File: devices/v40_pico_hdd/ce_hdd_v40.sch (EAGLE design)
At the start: 110 parts, among them IC1 RASPBERRY_PICOSMD-TH, IC101 74LVC245AT20-13, IC2 74LVC245AT20-13, IC201 74LVC245AT20-13, IC202 74LVC373APW,118, IC203 74LVC373APW,118, IC204 AZ1117H-ADJTRE1, IC3 74LVC245AT20-13, IC4 TLV1117LV33DCYR, IC5 74LVC245AT20-13, IC6 74AHCT1G08GW,125, J101 M19, J2 USB4125-GF-A, J201 TE Connectivity - 5173280-3, J203 ZL231-50PG, Q201 FDV304P, Q202 FDV304P, Q203 FDV304P, Q204 FDV304P, Q205 FDV304P, Q206 FDV304P, Q207 FDV304P, Q208 FDV304P, Q209 FDV304P, Q210 FDV304P, Q211 FDV304P, Q212 FDV304P, Q213 FDV304P, Q214 FDV304P, Q215 FDV304P, Q216 FDV304P, Q217 FDV304P, Q218 FDV304P, SW1 SMSR-1

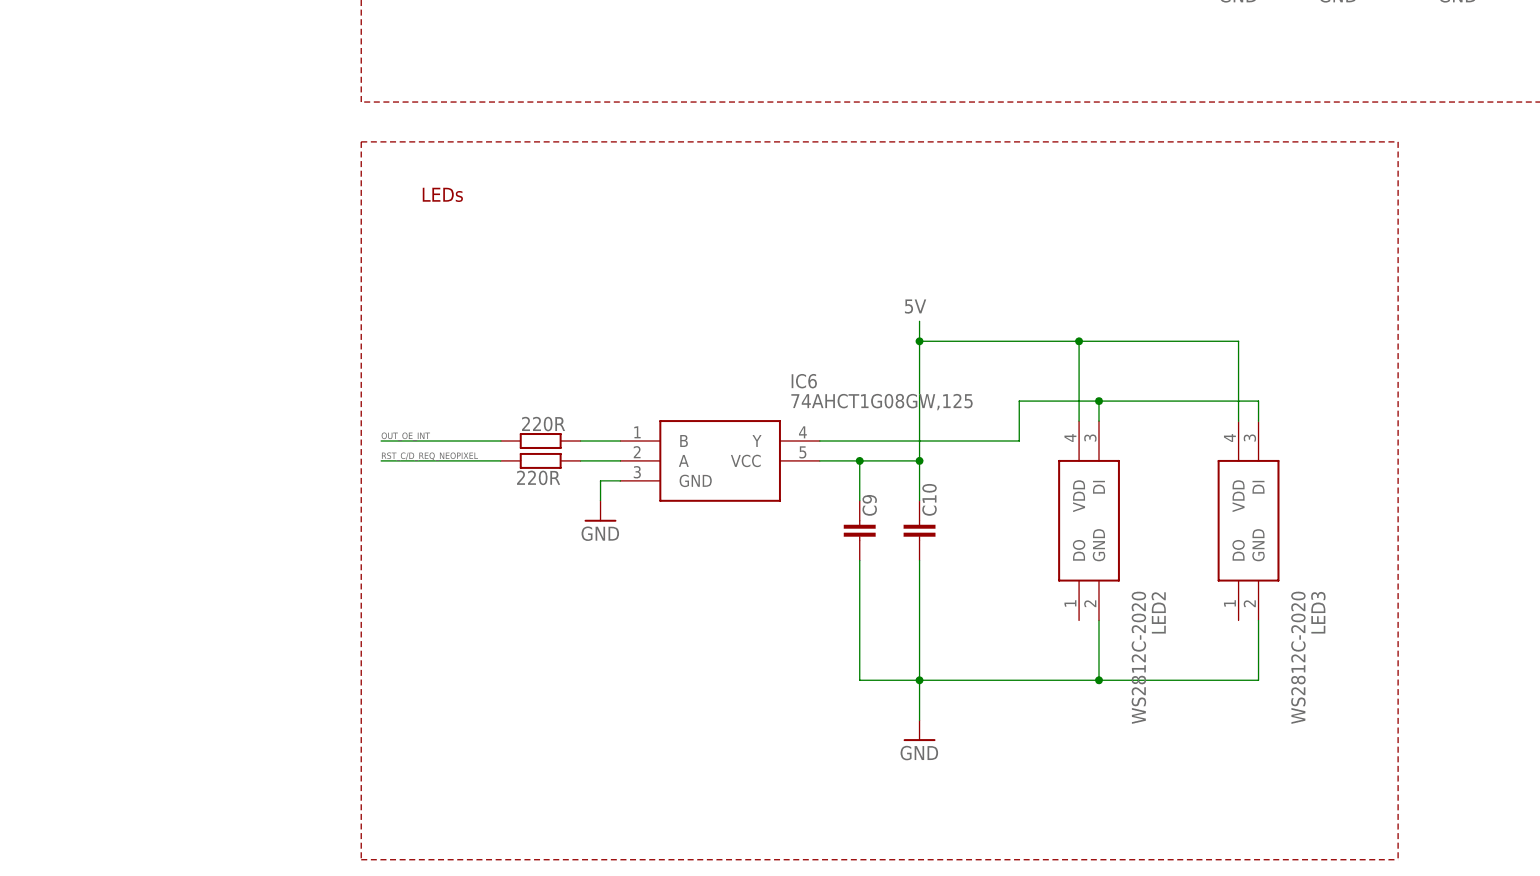
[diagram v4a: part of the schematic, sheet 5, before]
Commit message: fix for SCSI neopixel colors during start / run
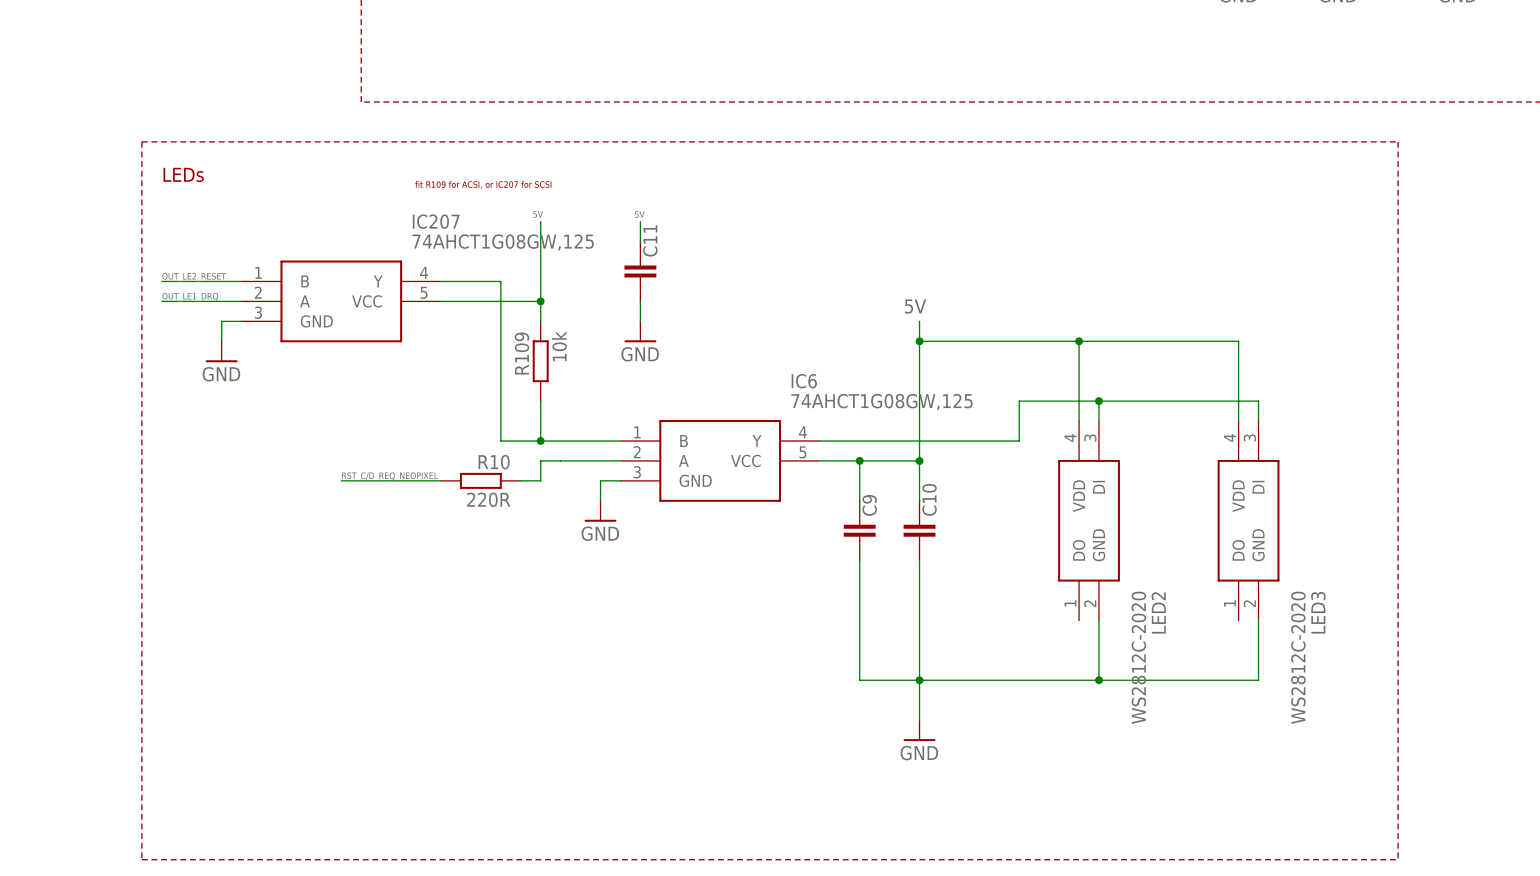
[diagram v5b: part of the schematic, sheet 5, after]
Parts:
- removed R9: 220R, rcl:R-EU_R0603
- added C11: 100 nF, rcl:C-EUC0603
- added IC207: 74AHCT1G08GW,125, 74AHCT1G08GW_125:74AHCT1G08GW,125
- added R109: 10k, rcl:R-EU_R0603
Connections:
- net 5V: now also C11.1, IC207.VCC, R109.1
- net GND: now also C11.2, IC207.GND
- net N$4: now also IC207.Y, R109.2; no longer R9.2
- net OUT_LE1_DRQ: now also IC207.A
- net OUT_LE2_RESET: now also IC207.B
- net OUT_OE_INT: no longer R9.1
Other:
- note added: "fit R109 for ACSI, or IC207 for SCSI"
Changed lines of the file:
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@@
 <part name="R8" library="rcl" deviceset="R-EU_" device="R0603" value="10k"/>
 <part name="IC6" library="74AHCT1G08GW_125" deviceset="74AHCT1G08GW,125" device=""/>
-<part name="R9" library="rcl" deviceset="R-EU_" device="R0603" value="220R"/>
 <part name="D101" library="BAT54WSTR" deviceset="BAT54WSTR" device="">
 <variant name="SCSI" populate="no"/>
@@
 <variant name="SCSI" populate="no"/>
 </part>
+<part name="IC207" library="74AHCT1G08GW_125" deviceset="74AHCT1G08GW,125" device="">
+<attribute name="DESCRIPTION" value="74AHC(T)1G08 - 2-input AND gate@en-us"/>
+<attribute name="HEIGHT" value="1.1mm"/>
+<attribute name="MANUFACTURER_NAME" value="Nexperia"/>
+<attribute name="MANUFACTURER_PART_NUMBER" value="74AHCT1G08GW,125"/>
+<attribute name="TME_ELECTRONIC_COMPONENTS_PART_NUMBER" value=""/>
+<attribute name="TME_ELECTRONIC_COMPONENTS_PRICE-STOCK" value=""/>
+<variant name="ACSI" populate="no"/>
+</part>
+<part name="GND22" library="supply1" deviceset="GND" device=""/>
+<part name="R109" library="rcl" deviceset="R-EU_" device="R0603" value="10k">
+<variant name="SCSI" populate="no" value="220R"/>
+</part>
+<part name="C11" library="rcl" deviceset="C-EU" device="C0603" value="100 nF"/>
+<part name="GND23" library="supply1" deviceset="GND" device=""/>
 </parts>
 <sheets>
@@
 <wire x1="109.22" y1="88.9" x2="109.22" y2="231.14" width="0.1524" layer="94" style="shortdash"/>
 <text x="116.84" y="223.52" size="2.54" layer="94" font="vector">power supply</text>
-<wire x1="109.22" y1="83.82" x2="241.3" y2="83.82" width="0.1524" layer="94" style="shortdash"/>
-<wire x1="109.22" y1="83.82" x2="109.22" y2="-7.62" width="0.1524" layer="94" style="shortdash"/>
+<wire x1="81.28" y1="83.82" x2="241.3" y2="83.82" width="0.1524" layer="94" style="shortdash"/>
+<wire x1="81.28" y1="83.82" x2="81.28" y2="-7.62" width="0.1524" layer="94" style="shortdash"/>
 <wire x1="241.3" y1="83.82" x2="241.3" y2="-7.62" width="0.1524" layer="94" style="shortdash"/>
-<wire x1="109.22" y1="-7.62" x2="241.3" y2="-7.62" width="0.1524" layer="94" style="shortdash"/>
+<wire x1="81.28" y1="-7.62" x2="241.3" y2="-7.62" width="0.1524" layer="94" style="shortdash"/>
 <text x="-63.5" y="116.078" size="0.8128" layer="91" font="vector" ratio="10">If using W6100, GP15 and GP22 can be used for IKBD</text>
 <text x="-63.5" y="114.3" size="0.8128" layer="94" font="vector" ratio="10">If using W6300, GP15 and GP22 are used by W6300 and IKBD cannot use them.</text>
@@
 <text x="79.502" y="154.178" size="0.8128" layer="91" font="vector" rot="R90">fit for ACSI</text>
 <text x="79.502" y="138.43" size="0.8128" layer="91" font="vector" rot="R90">fit for SCSI</text>
-<text x="116.84" y="76.2" size="1.778" layer="94">LEDs</text>
+<text x="83.82" y="78.74" size="1.778" layer="94">LEDs</text>
+<text x="116.078" y="77.978" size="0.8128" layer="94" font="vector">fit R109 for ACSI, or IC207 for SCSI</text>
 </plain>
 <instances>
@@
 </instance>
 <instance part="GND11" gate="1" x="76.2" y="132.08"/>
-<instance part="R10" gate="G$1" x="132.08" y="43.18" smashed="yes" rot="MR0">
-<attribute name="VALUE" x="134.62" y="40.132" size="1.778" layer="96" rot="MR0"/>
-</instance>
+<instance part="R10" gate="G$1" x="124.46" y="40.64" rot="MR0"/>
 <instance part="SW1" gate="G$1" x="198.12" y="137.16"/>
 <instance part="LED3" gate="G$1" x="223.52" y="48.26" rot="R270"/>
@@
 </instance>
 <instance part="IC6" gate="G$1" x="142.24" y="45.72"/>
-<instance part="R9" gate="G$1" x="132.08" y="45.72" smashed="yes" rot="MR180">
-<attribute name="VALUE" x="129.54" y="48.768" size="1.778" layer="96" rot="MR180"/>
+<instance part="IC207" gate="G$1" x="93.98" y="66.04"/>
+<instance part="GND22" gate="1" x="91.44" y="55.88"/>
+<instance part="R109" gate="G$1" x="132.08" y="55.88" rot="MR270"/>
+<instance part="C11" gate="G$1" x="144.78" y="68.58" smashed="yes">
+<attribute name="NAME" x="146.939" y="69.088" size="1.778" layer="95" rot="R90"/>
 </instance>
+<instance part="GND23" gate="1" x="144.78" y="58.42"/>
 </instances>
 <busses>
@@
 <wire x1="76.2" y1="137.16" x2="76.2" y2="134.62" width="0.1524" layer="91"/>
 </segment>
+<segment>
+<pinref part="IC207" gate="G$1" pin="GND"/>
+<pinref part="GND22" gate="1" pin="GND"/>
+<wire x1="93.98" y1="60.96" x2="91.44" y2="60.96" width="0.1524" layer="91"/>
+<wire x1="91.44" y1="60.96" x2="91.44" y2="58.42" width="0.1524" layer="91"/>
+</segment>
+<segment>
+<pinref part="C11" gate="G$1" pin="2"/>
+<pinref part="GND23" gate="1" pin="GND"/>
+<wire x1="144.78" y1="63.5" x2="144.78" y2="60.96" width="0.1524" layer="91"/>
+</segment>
 </net>
 <net name="5V" class="0">
@@
 <pinref part="IC6" gate="G$1" pin="VCC"/>
 </segment>
+<segment>
+<pinref part="IC207" gate="G$1" pin="VCC"/>
+<wire x1="119.38" y1="63.5" x2="132.08" y2="63.5" width="0.1524" layer="91"/>
+<wire x1="132.08" y1="63.5" x2="132.08" y2="73.66" width="0.1524" layer="91"/>
+<label x="131.064" y="74.168" size="0.8128" layer="95" font="vector"/>
+<pinref part="R109" gate="G$1" pin="1"/>
+<wire x1="132.08" y1="60.96" x2="132.08" y2="63.5" width="0.1524" layer="91"/>
+<junction x="132.08" y="63.5"/>
+</segment>
+<segment>
+<pinref part="C11" gate="G$1" pin="1"/>
+<wire x1="144.78" y1="71.12" x2="144.78" y2="73.66" width="0.1524" layer="91"/>
+<label x="144.018" y="74.168" size="0.8128" layer="95" font="vector"/>
+</segment>
 </net>
 <net name="N$1" class="0">
@@
 <segment>
 <pinref part="R10" gate="G$1" pin="2"/>
-<wire x1="127" y1="43.18" x2="111.76" y2="43.18" width="0.1524" layer="91"/>
-<label x="111.76" y="43.434" size="0.8128" layer="95" font="vector"/>
+<wire x1="119.38" y1="40.64" x2="106.68" y2="40.64" width="0.1524" layer="91"/>
+<label x="106.68" y="40.894" size="0.8128" layer="95" font="vector"/>
 </segment>
 </net>
@@
 <pinref part="R8" gate="G$1" pin="2"/>
 </segment>
+<segment>
+<pinref part="IC207" gate="G$1" pin="A"/>
+<wire x1="93.98" y1="63.5" x2="83.82" y2="63.5" width="0.1524" layer="91"/>
+<label x="83.82" y="63.754" size="0.8128" layer="95" font="vector"/>
+</segment>
 </net>
 <net name="SEL_I/O_DP_A1" class="0">
@@
 <pinref part="R7" gate="G$1" pin="2"/>
 </segment>
-<segment>
-<pinref part="R9" gate="G$1" pin="1"/>
-<wire x1="127" y1="45.72" x2="111.76" y2="45.72" width="0.1524" layer="91"/>
-<label x="111.76" y="45.974" size="0.8128" layer="95" font="vector"/>
-</segment>
 </net>
 <net name="OUT_LE2_RESET" class="0">
@@
 <label x="-18.796" y="127.254" size="0.8128" layer="95" font="vector"/>
 </segment>
+<segment>
+<pinref part="IC207" gate="G$1" pin="B"/>
+<wire x1="93.98" y1="66.04" x2="83.82" y2="66.04" width="0.1524" layer="91"/>
+<label x="83.82" y="66.294" size="0.8128" layer="95" font="vector"/>
+</segment>
 </net>
 <net name="KEYB_RX" class="0">
@@
 <segment>
 <pinref part="R10" gate="G$1" pin="1"/>
-<wire x1="137.16" y1="43.18" x2="142.24" y2="43.18" width="0.1524" layer="91"/>
+<wire x1="129.54" y1="40.64" x2="132.08" y2="40.64" width="0.1524" layer="91"/>
+<wire x1="132.08" y1="40.64" x2="132.08" y2="43.18" width="0.1524" layer="91"/>
+<wire x1="132.08" y1="43.18" x2="134.62" y2="43.18" width="0.1524" layer="91"/>
+<wire x1="134.62" y1="43.18" x2="142.24" y2="43.18" width="0.1524" layer="91"/>
 <pinref part="IC6" gate="G$1" pin="A"/>
 </segment>
@@
 <segment>
 <pinref part="IC6" gate="G$1" pin="B"/>
-<pinref part="R9" gate="G$1" pin="2"/>
-<wire x1="142.24" y1="45.72" x2="137.16" y2="45.72" width="0.1524" layer="91"/>
+<pinref part="IC207" gate="G$1" pin="Y"/>
+<wire x1="119.38" y1="66.04" x2="127" y2="66.04" width="0.1524" layer="91"/>
+<wire x1="127" y1="66.04" x2="127" y2="45.72" width="0.1524" layer="91"/>
+<wire x1="127" y1="45.72" x2="132.08" y2="45.72" width="0.1524" layer="91"/>
+<pinref part="R109" gate="G$1" pin="2"/>
+<wire x1="132.08" y1="45.72" x2="142.24" y2="45.72" width="0.1524" layer="91"/>
+<wire x1="132.08" y1="50.8" x2="132.08" y2="45.72" width="0.1524" layer="91"/>
+<junction x="132.08" y="45.72"/>
 </segment>
 </net>

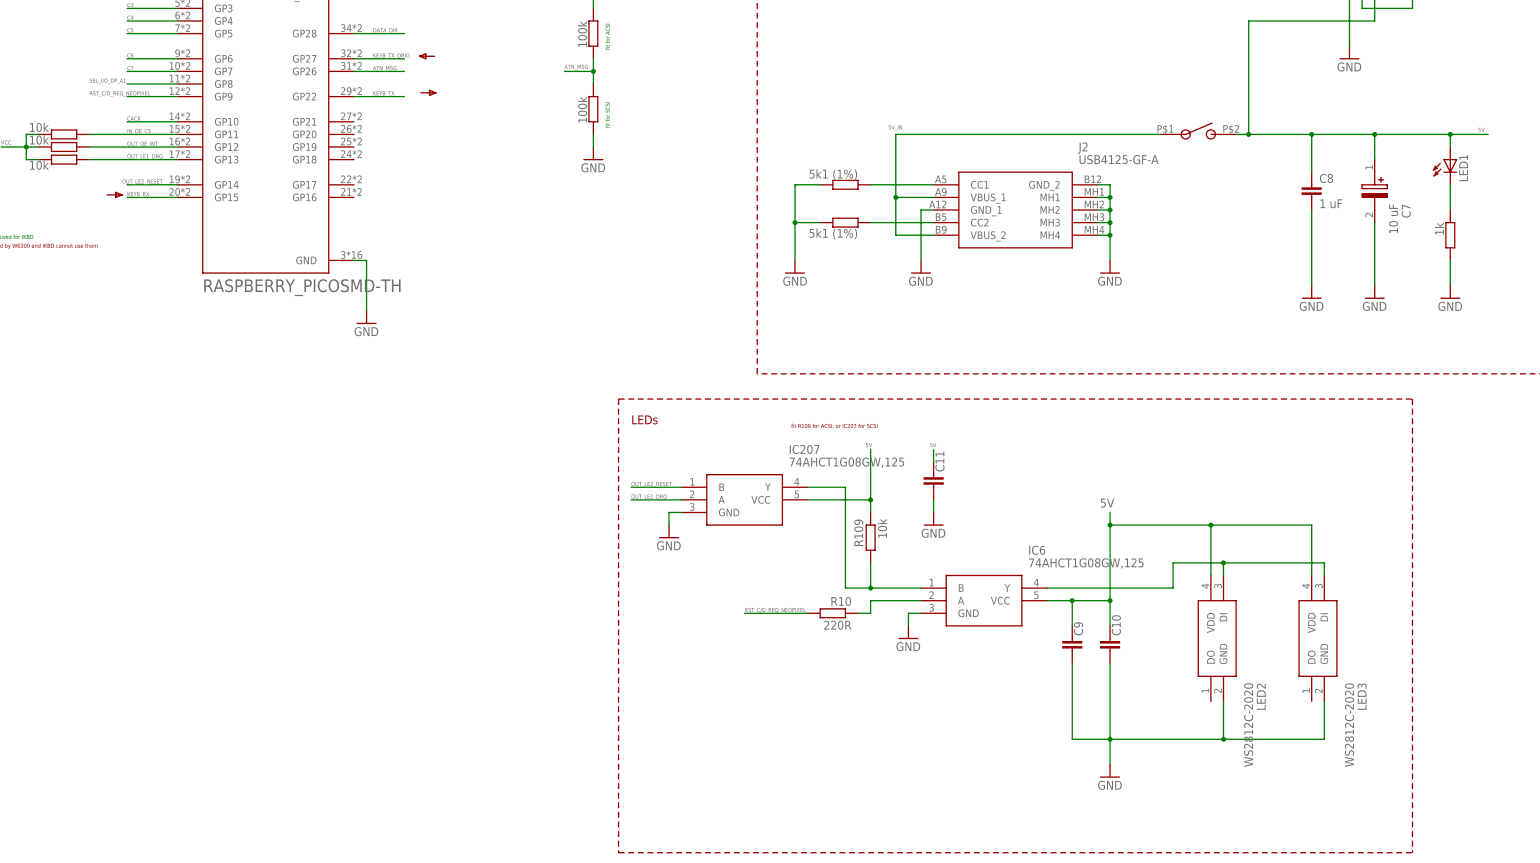
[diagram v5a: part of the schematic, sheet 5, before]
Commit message: hdd pcb has now different led connections for scsi and for acsi
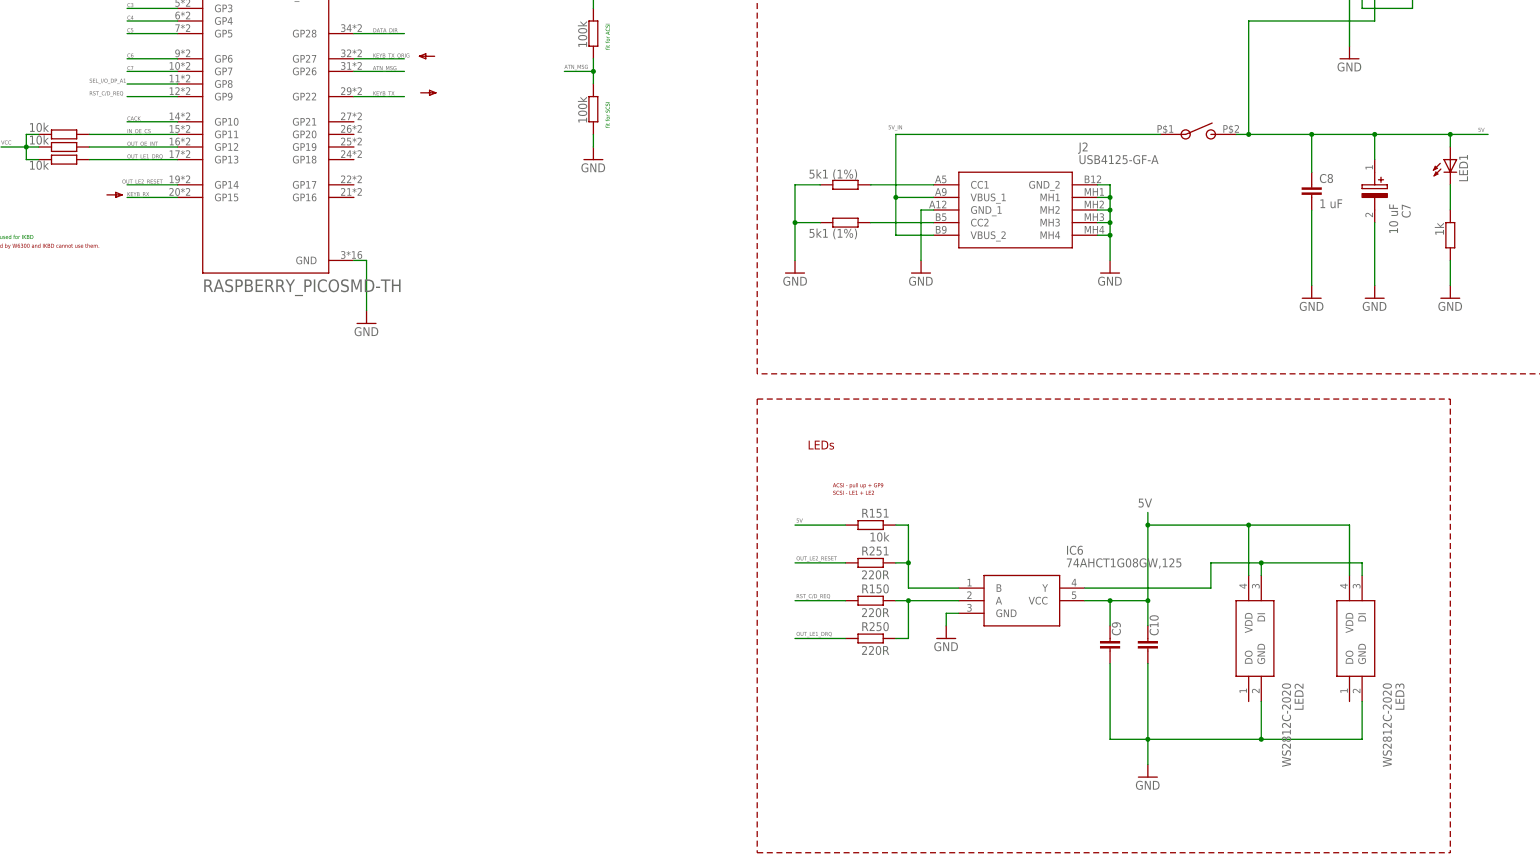
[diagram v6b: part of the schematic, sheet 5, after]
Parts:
- removed C11: 100 nF, rcl:C-EUC0603
- removed IC207: 74AHCT1G08GW,125, 74AHCT1G08GW_125:74AHCT1G08GW,125
- removed R10: 220R, rcl:R-EU_R0603
- removed R109: 10k, rcl:R-EU_R0603
- added R150, R250, R251: 220R, rcl:R-EU_R0603
- added R151: 10k, rcl:R-EU_R0603
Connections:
- removed net RST_C/D_REQ_NEOPIXEL: IC1.GP9, IC201.B2, IC202.D1, IC202.D6, IC203.D0, IC203.D7, R10.2
- new net RST_C/D_REQ: IC1.GP9, IC201.B2, IC202.D1, IC202.D6, IC203.D0, IC203.D7, R150.2
- net 5V: now also R151.2; no longer C11.1, IC207.VCC, R109.1
- net GND: no longer C11.2, IC207.GND
- net N$3: now also R150.1, R250.1; no longer R10.1
- net N$4: now also R151.1, R251.1; no longer IC207.Y, R109.2
- net OUT_LE1_DRQ: now also R250.2; no longer IC207.A
- net OUT_LE2_RESET: now also R251.2; no longer IC207.B
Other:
- note added: "ACSI - pull up + GP9"
- note added: "SCSI - LE1 + LE2"
- note removed: "fit R109 for ACSI, or IC207 for SCSI"
- moved on the sheet: C10, C9, IC6, LED2, LED3
